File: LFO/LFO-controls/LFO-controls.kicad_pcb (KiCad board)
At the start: 2 copper layers, 30 x 114.5 mm, 21 parts, among them J1 AudioJack2, J10 Conn_01x06, J11 Conn_01x01, J12 Conn_01x01, J13 Conn_01x01, J14 Conn_01x01, J15 Conn_01x03, J2 AudioJack2, J3 AudioJack2, J4 AudioJack2, J5 AudioJack2, J6 AudioJack2, J7 AudioJack2, J8 AudioJack2, J9 Conn_01x06

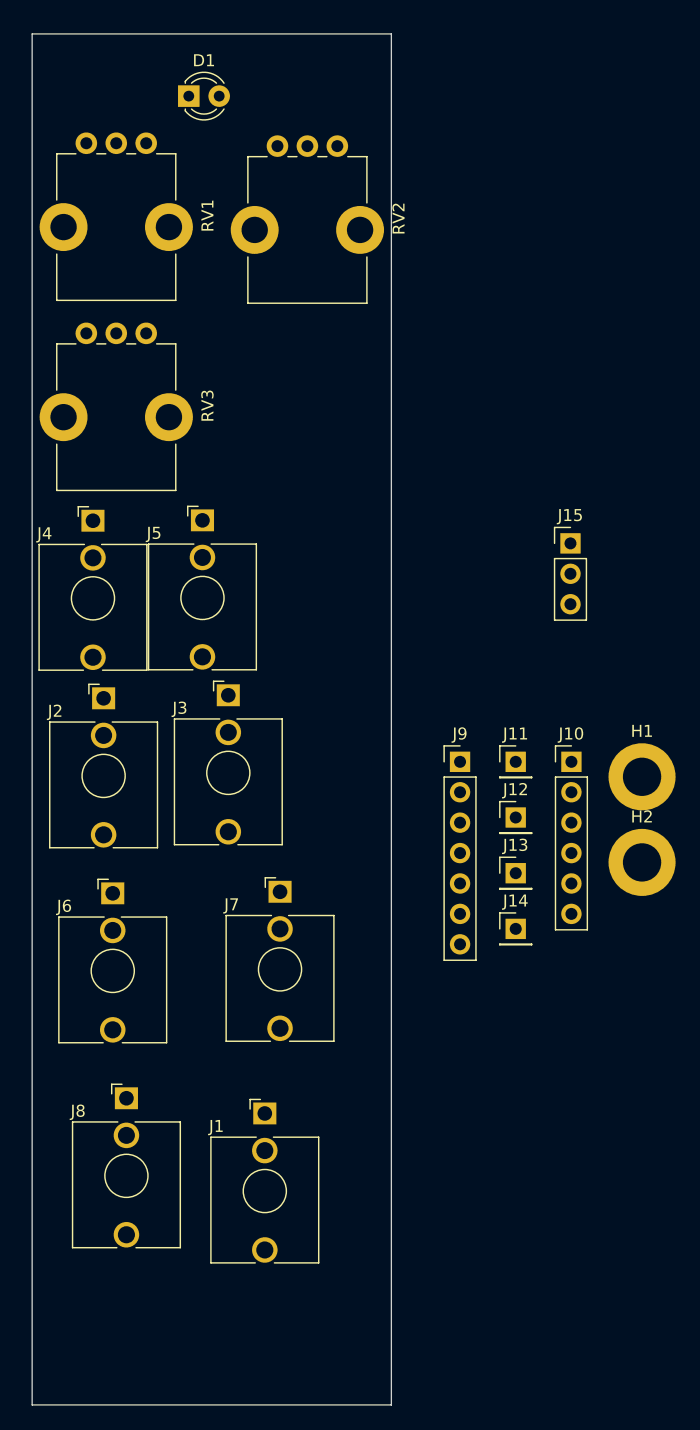
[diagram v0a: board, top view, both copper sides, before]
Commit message: LFO panel, not fully routed
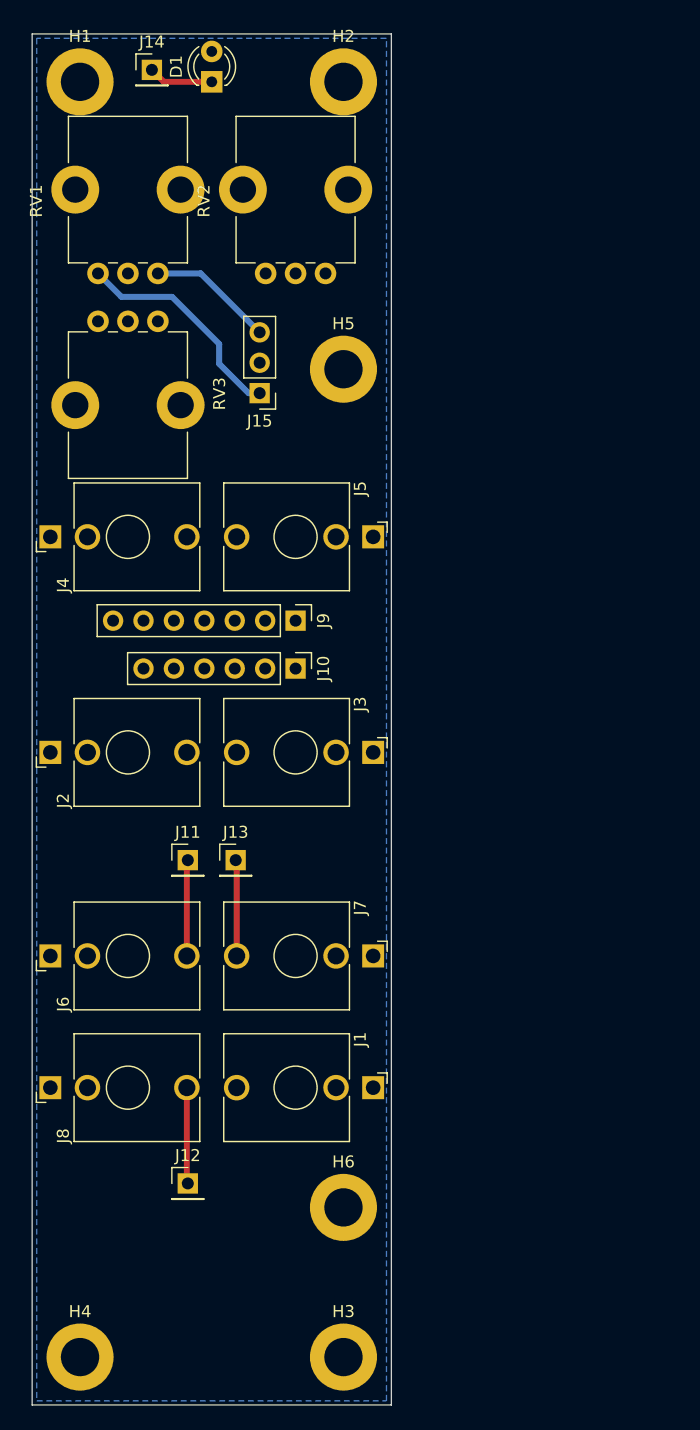
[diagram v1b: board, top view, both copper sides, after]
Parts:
- added H3: MountingHole_Pad, MountingHole:MountingHole_3.2mm_M3_DIN965_Pad, F.Cu at (26.0, 117.5)
- added H4: MountingHole_Pad, MountingHole:MountingHole_3.2mm_M3_DIN965_Pad, F.Cu at (4.00, 117.5)
- added H5: MountingHole_Pad, MountingHole:MountingHole_3.2mm_M3_DIN965_Pad, F.Cu at (26.0, 35.0)
- added H6: MountingHole_Pad, MountingHole:MountingHole_3.2mm_M3_DIN965_Pad, F.Cu at (26.0, 105.0)
- moved J14 77.9 mm to (10.0, 10.0)
- moved H1 74.6 mm to (4.00, 11.0)
- moved H2 69.8 mm to (26.0, 11.0)
- moved J12 41.0 mm to (13.0, 103.0)
- moved J15 28.8 mm to (19.0, 37.0), turned to 180 degrees
- moved J11 28.6 mm to (13.0, 76.0)
- moved J10 24.3 mm to (22.0, 60.0), turned to -90 degrees
- moved J13 23.4 mm to (17.0, 76.0)
- moved J9 18.1 mm to (22.0, 56.0), turned to -90 degrees
- moved J5 9.30 mm to (22.0, 49.0), turned to -90 degrees
- moved J1 9.01 mm to (22.0, 95.0), turned to -90 degrees
- moved J8 7.37 mm to (8.00, 95.0), turned to 90 degrees
- moved J4 5.91 mm to (8.00, 49.0), turned to 90 degrees
- moved J3 5.87 mm to (22.0, 67.0), turned to -90 degrees
- moved RV2 3.51 mm to (22.0, 20.0), turned to 180 degrees
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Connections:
- RV1 pad : (no net) -> GND
- RV2 pad : (no net) -> GND
- RV3 pad : (no net) -> GND
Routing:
- net +12V: track 0.00 -> 18.6 mm
- net -12V: track 0.00 -> 10.5 mm
- net TRI: track 0.00 -> 8.03 mm
- net SAW: track 0.00 -> 8.03 mm
- net SIN: track 0.00 -> 8.03 mm
- net LEDA: track 0.00 -> 5.41 mm
- added copper zone on B.Cu, net GND

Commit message: LFO controls completed
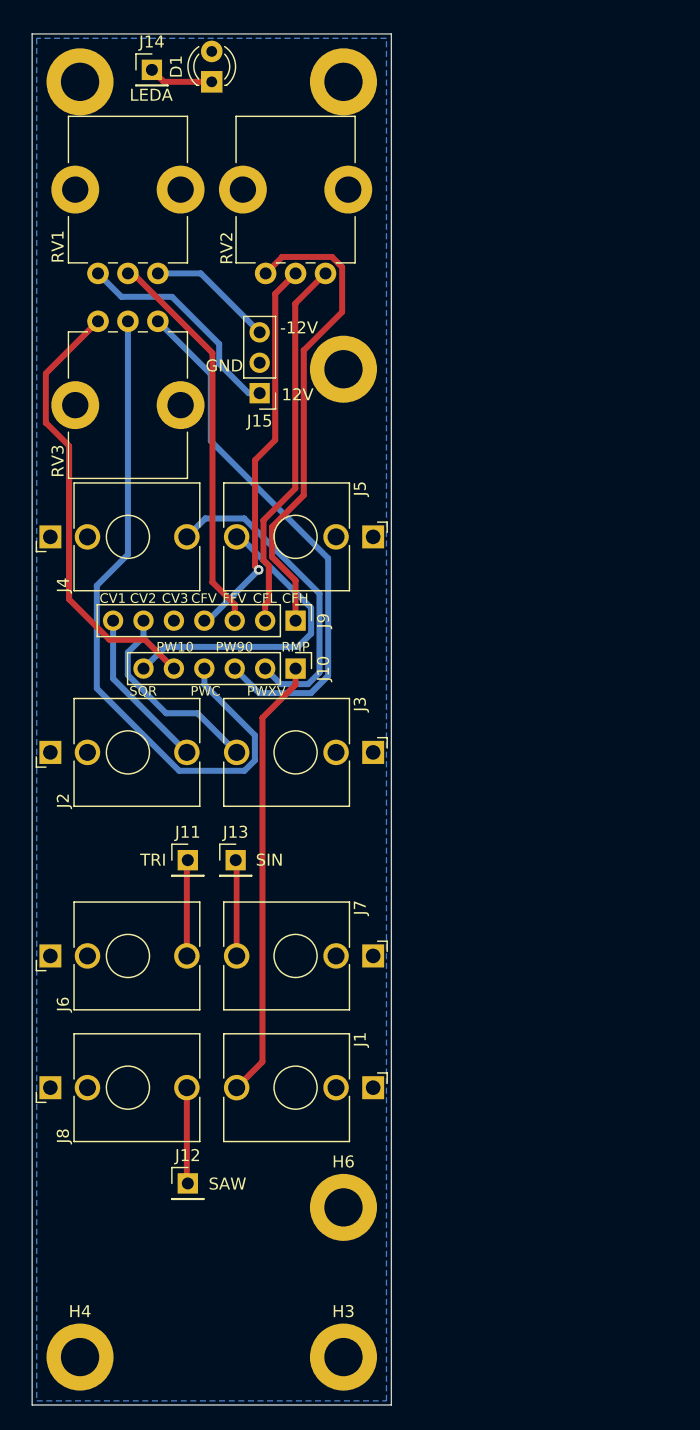
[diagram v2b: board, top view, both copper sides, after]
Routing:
- net PWC: track 0.00 -> 57.6 mm
- net PW90: track 0.00 -> 44.7 mm
- net CFH: track 0.00 -> 40.1 mm
- net RMP: track 0.00 -> 37.0 mm
- net PW10: track 0.00 -> 37.0 mm
- net FFV: track 0.00 -> 32.9 mm
- net CFV: track 0.00 -> 32.6 mm, vias 0 -> 1
- net CFL: track 0.00 -> 31.5 mm
- net PWXV: track 0.00 -> 26.4 mm
- net SQR: track 0.00 -> 26.0 mm
- net CV2: track 0.00 -> 16.8 mm
- net CV1: track 0.00 -> 13.6 mm
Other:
- board text added: "-12V"
- board text added: "12V"
- board text added: "CFH"
- board text added: "CFL"
- board text added: "CFV"
- board text added: "CV1"
- board text added: "CV2"
- board text added: "CV3"
- board text added: "FFV"
- board text added: "GND"
- board text added: "LEDA"
- board text added: "PW10"
- board text added: "PW90"
- board text added: "PWC"
- board text added: "PWXV"
- board text added: "RMP"
- board text added: "SAW"
- board text added: "SIN"
- board text added: "SQR"
- board text added: "TRI"

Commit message: minor fixes after first build
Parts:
- moved COARSE1 14.0 mm to (8.00, 20.0)
- moved FINE1 14.0 mm to (22.0, 20.0)
- renumbered RV2 to COARSE1, RV1 to FINE1, J2 to J1, J3 to J2, J4 to J3, J5 to J4, J6 to J5, J7 to J6, J8 to J7, J1 to J8, RV3 to PW1
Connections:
- COARSE1 pad : GND -> (no net)
- COARSE1 pad 1: CFL -> CFH
- COARSE1 pad 3: CFH -> CFL
- FINE1 pad : GND -> (no net)
- PW1 pad : GND -> (no net)
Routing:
- net +12V: track 18.6 -> 10.9 mm
- net CFL: track 31.5 -> 37.5 mm
- net CFV: track 32.6 -> 35.9 mm, vias 1 -> 0
- net -12V: track 10.5 -> 13.1 mm
- net CFH: track 40.1 -> 38.2 mm, vias 0 -> 1
- net FFV: track 32.9 -> 31.1 mm
- net PWC: track 57.6 -> 57.7 mm, vias 0 -> 1

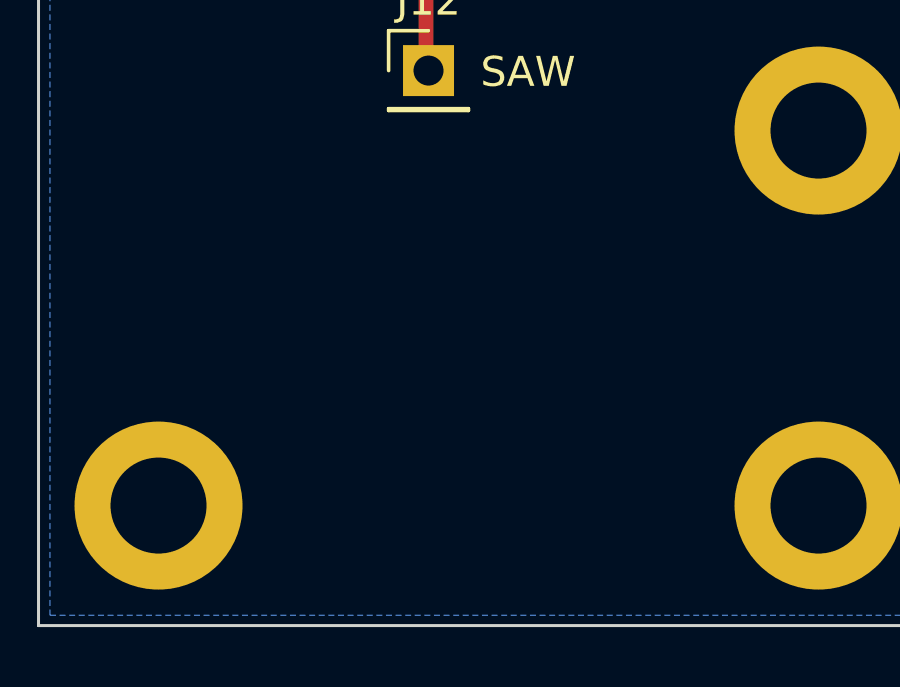
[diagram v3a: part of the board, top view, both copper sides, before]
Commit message: minor cleanup of silkscreen
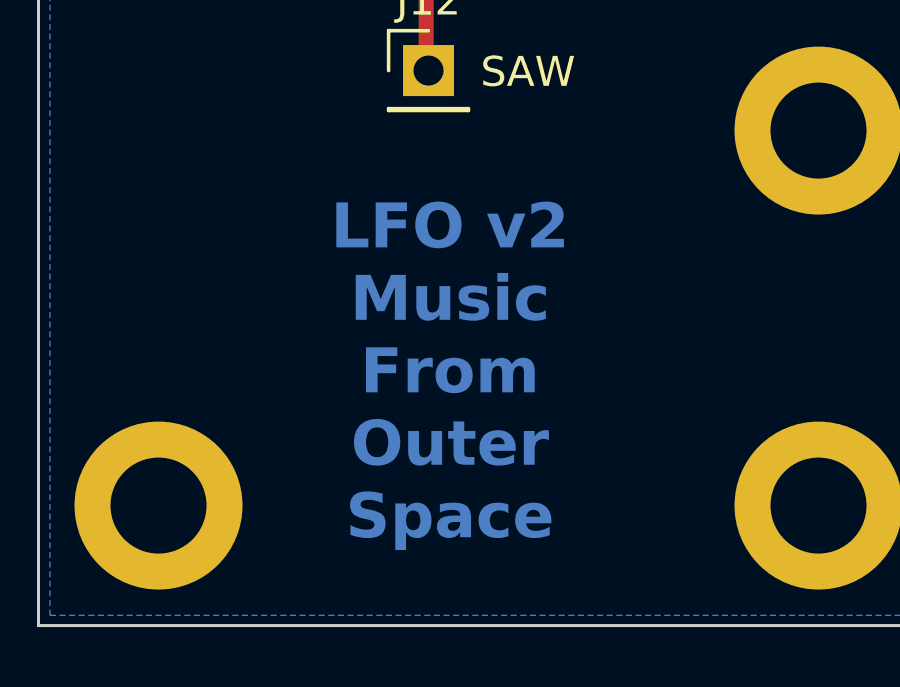
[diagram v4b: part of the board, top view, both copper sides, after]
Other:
- board text added: "LFO v2 Music From Outer Space"
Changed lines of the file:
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@@
   (gr_rect (start 0 7) (end 30 121.5)
     (stroke (width 0.1) (type default)) (fill none) (layer "Edge.Cuts"))
+  (gr_text "LFO v2\nMusic\nFrom\nOuter\nSpace" (at 13.716 113.03) (layer "B.Cu")
+    (effects (font (size 1.5 1.5) (thickness 0.3) bold))
+  )
   (gr_text "LEDA" (at 9.906 11.43) (layer "B.SilkS")
     (effects (font (size 1 1) (thickness 0.15)) (justify top mirror))
